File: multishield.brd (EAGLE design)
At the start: 57.6 x 53.7 mm, 21 parts, among them J1 7p-2.54-90d, J2 2x16p-2.54, J3 7p-2.54-90d, J4 2x6p-2.54, J5 7p-2.54-90d, J6 7p-2.54-90d, K2 TS-1101F, M1 ARDUINO_R3_ICSP, SW1 SK-12D01, U1 AD595AQ-DIP14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

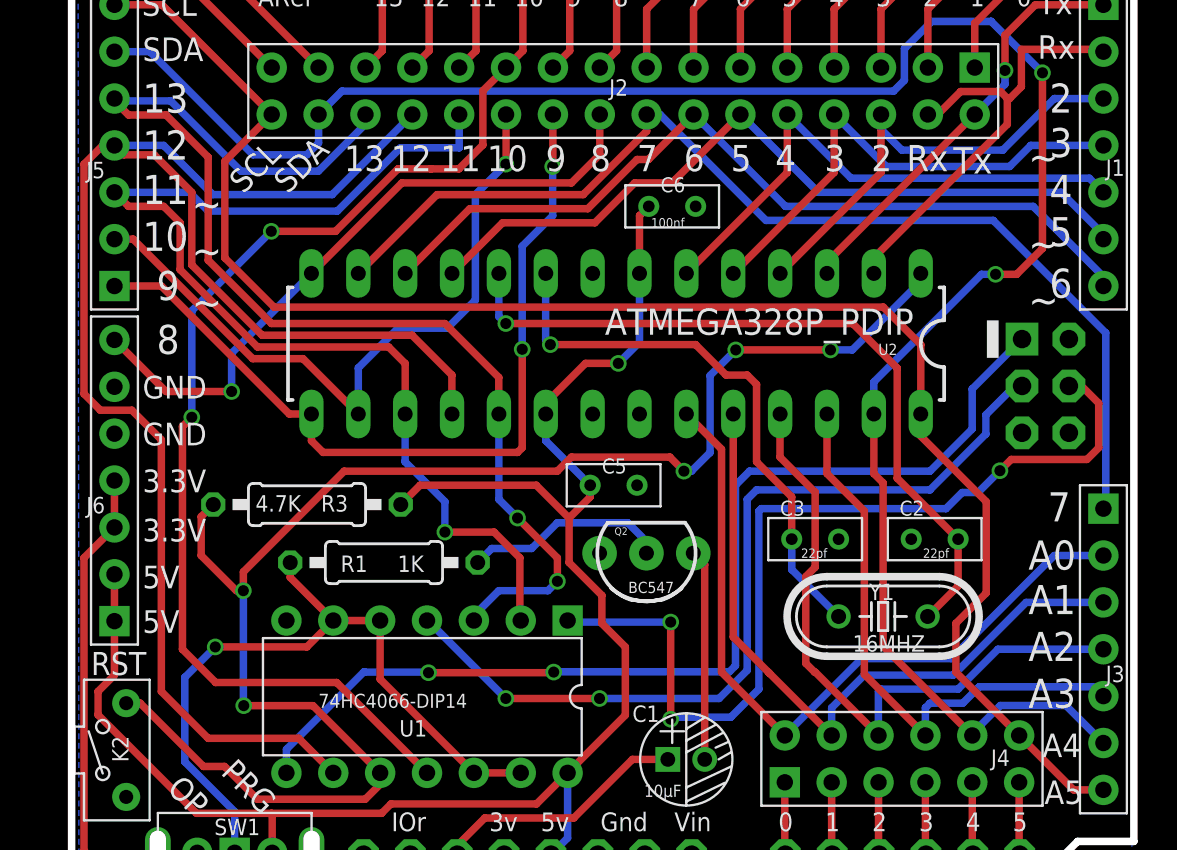
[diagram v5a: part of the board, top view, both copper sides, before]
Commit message: moved atmega328 further to the left
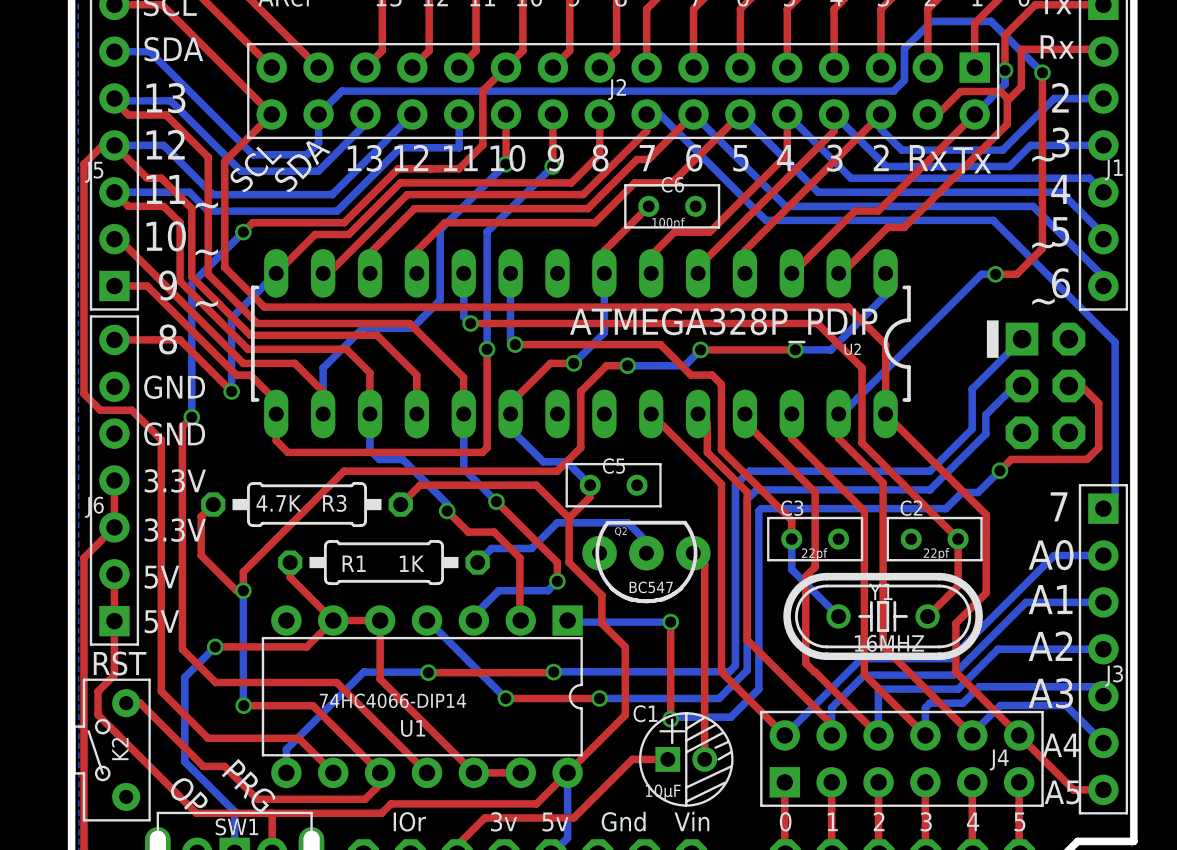
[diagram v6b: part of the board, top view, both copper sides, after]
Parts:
- moved U2 1.91 mm to (30.4, 30.5)
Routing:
- net SLAVE-RESET: track 85.9 -> 83.1 mm
- net N$30: track 41.9 -> 44.5 mm
- net N$41: track 45.6 -> 48.1 mm
- net N$32: track 59.1 -> 61.2 mm
- net MISO: track 91.4 -> 89.4 mm
- net VCC: track 91.8 -> 93.9 mm
- net N$29: track 29.8 -> 31.7 mm
- net N$49: track 110.4 -> 112.1 mm
- net N$25: track 22.9 -> 24.4 mm
- net N$26: track 25.0 -> 26.4 mm
- net N$33: track 36.2 -> 37.3 mm
- net MOSI: track 61.5 -> 60.5 mm
- net N$19: track 64.8 -> 65.7 mm
- net N$50: track 90.0 -> 89.2 mm
- net N$48: track 31.5 -> 32.2 mm
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
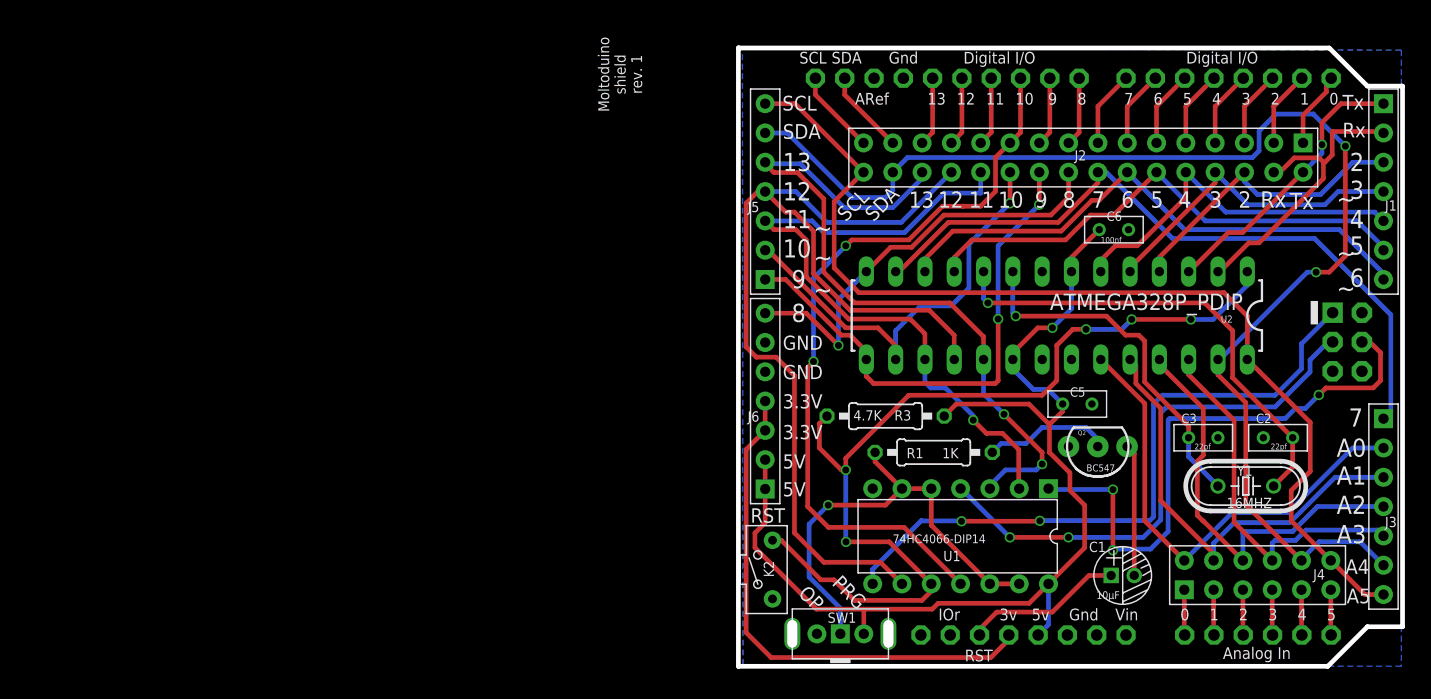
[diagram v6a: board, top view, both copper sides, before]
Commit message: 7-pin headers moved to the edges, some wiring refactored
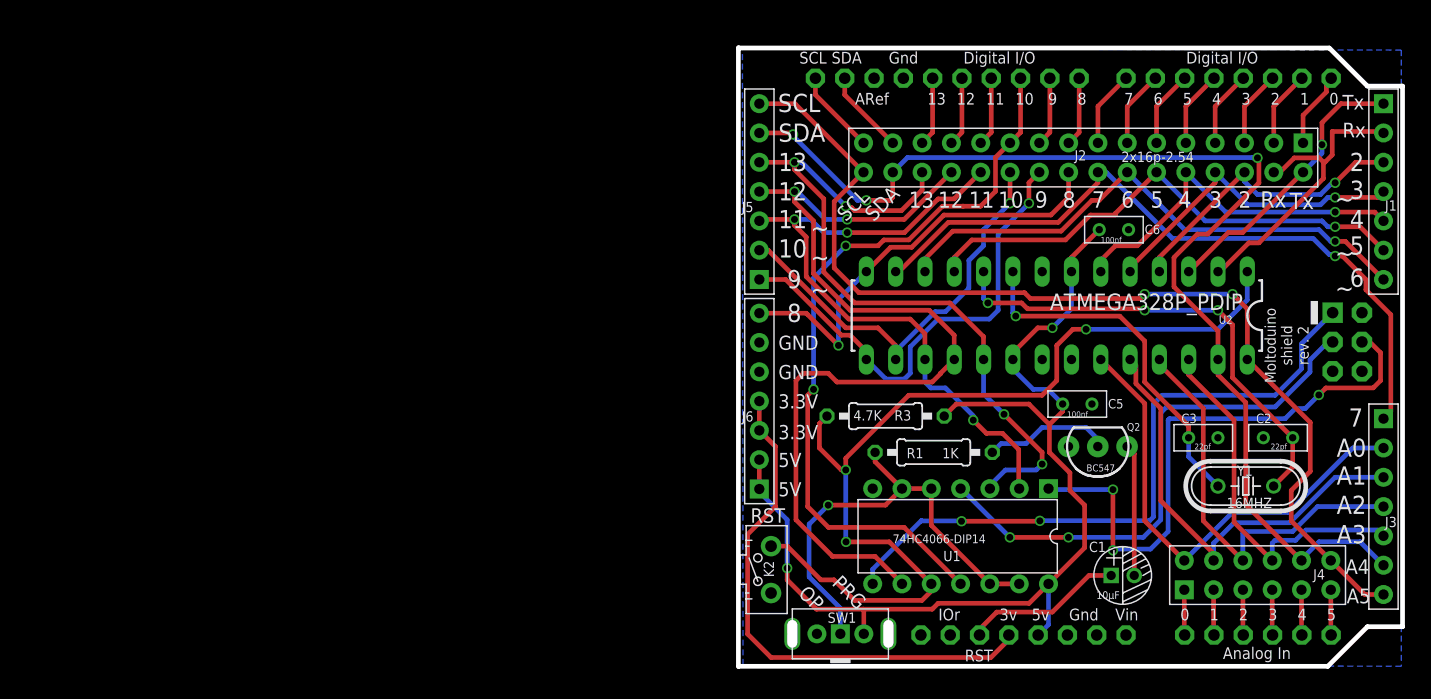
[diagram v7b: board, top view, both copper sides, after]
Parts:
- moved J5 0.51 mm to (4.57, 41.3)
- moved J6 0.51 mm to (4.57, 23.1)
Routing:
- net N$49: track 112.1 -> 100.3 mm, vias 2 -> 3
- net MISO: track 89.4 -> 82.4 mm, vias 0 -> 2
- net N$34: track 44.8 -> 41.9 mm, vias 2 -> 1
- net MOSI: track 60.5 -> 58.0 mm, vias 1 -> 3
- net N$50: track 89.2 -> 90.4 mm, vias 0 -> 2
- net SCK: track 64.5 -> 63.6 mm, vias 2 -> 4
- net N$54: track 45.5 -> 46.3 mm
- net SLAVE-RESET: track 83.1 -> 83.8 mm, vias 5 -> 3
- net N$35: track 37.8 -> 37.3 mm
- net VCC: track 93.9 -> 93.3 mm, vias 1 -> 2
- net N$32: track 61.2 -> 61.7 mm, vias 0 -> 1
- net N$33: track 37.3 -> 37.8 mm
- net N$55: track 41.4 -> 41.7 mm, vias 1 -> 3
- net N$41: track 48.1 -> 47.8 mm, vias 0 -> 1
- net N$30: track 44.5 -> 44.4 mm, vias 0 -> 1
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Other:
- board text added: "Moltoduino shield rev. 2"
- board text removed: "Moltoduino shield rev. 1"

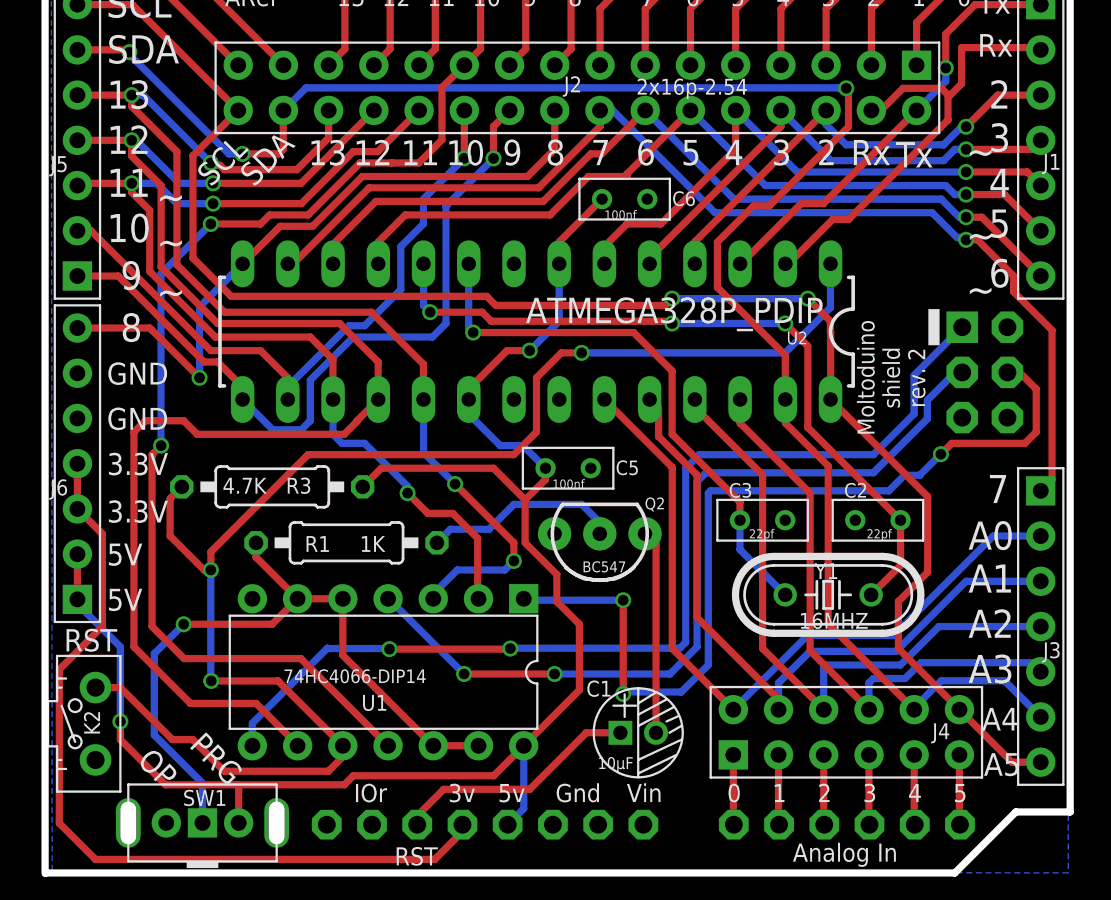
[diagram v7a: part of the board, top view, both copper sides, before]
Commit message: reset pin added, various changes (in pin packages to make soldering easier
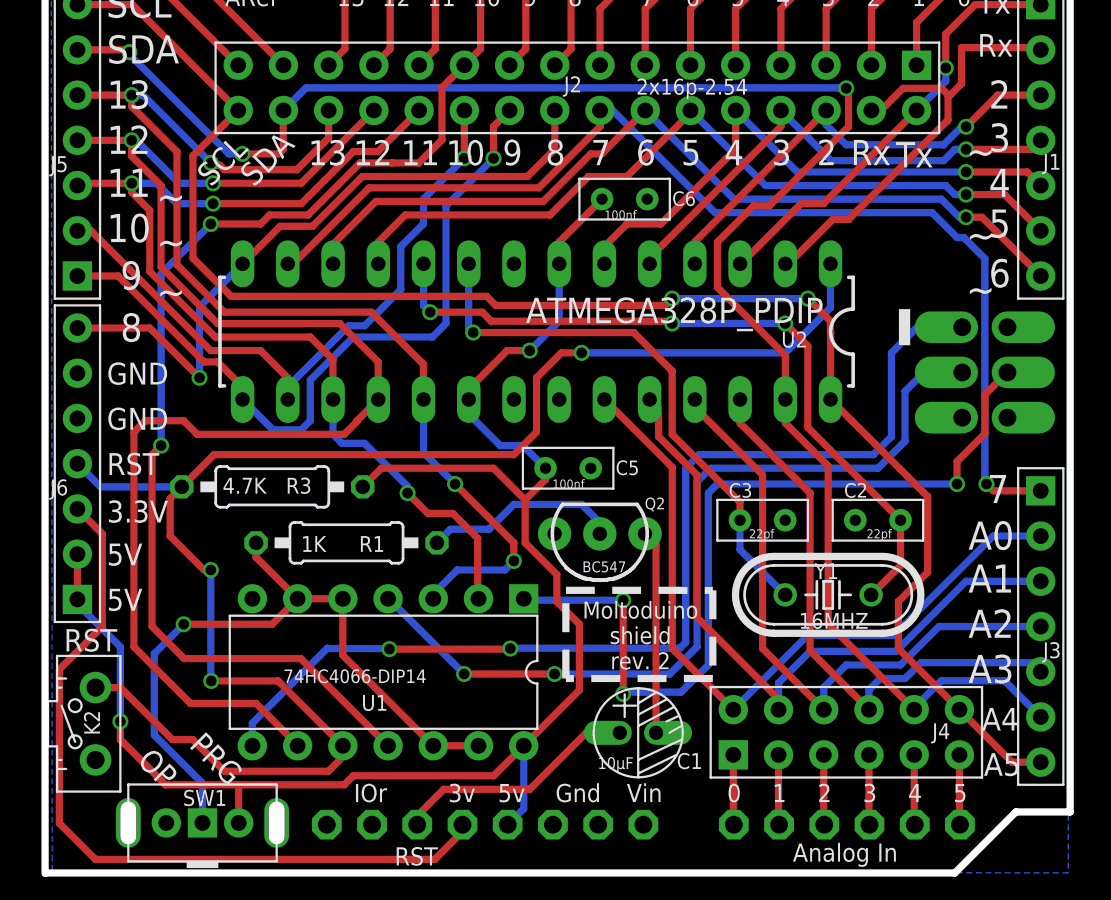
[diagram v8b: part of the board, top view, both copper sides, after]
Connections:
- net N$54: no longer J6.4
- net SLAVE-RESET: now also J6.4
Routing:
- net SLAVE-RESET: track 83.8 -> 89.3 mm
- net N$39: track 50.2 -> 47.6 mm
- net N$54: track 46.3 -> 43.8 mm
- net N$53: track 57.3 -> 58.8 mm
- net N$40: track 47.1 -> 48.1 mm
- net N$32: track 61.7 -> 62.6 mm
- net N$47: track 35.9 -> 35.3 mm
